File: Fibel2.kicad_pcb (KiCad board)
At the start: 2 copper layers, 210 x 148 mm, 0 parts

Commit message: added symbol&footprint for orin/sodimm, added a bunch of specs and docs, partially implemented audio, full steam ahead
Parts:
- added C1: 0.1uF, Capacitor_SMD:C_0603_1608Metric, F.Cu at (119.4, 76.9)
- added C10: 10uF, Capacitor_SMD:C_0603_1608Metric, F.Cu at (123.4, 84.5)
- added C11: 10uF, Capacitor_SMD:C_0603_1608Metric, F.Cu at (123.4, 87.0)
- added C12: 0.1uF, Capacitor_SMD:C_0603_1608Metric, F.Cu at (123.4, 89.5)
- added C13: 10uF, Capacitor_SMD:C_0603_1608Metric, F.Cu at (127.4, 76.9)
- added C14: 10uF, Capacitor_SMD:C_0603_1608Metric, F.Cu at (127.4, 79.4)
- added C15: 10uF, Capacitor_SMD:C_0603_1608Metric, F.Cu at (127.4, 81.9)
- added C16: 10uF, Capacitor_SMD:C_0603_1608Metric, F.Cu at (127.4, 84.5)
- added C17: 10uF, Capacitor_SMD:C_0603_1608Metric, F.Cu at (127.4, 87.0)
- added C18: 10uF, Capacitor_SMD:C_0603_1608Metric, F.Cu at (127.4, 89.5)
- added C19: 10uF, Capacitor_SMD:C_0603_1608Metric, F.Cu at (131.4, 76.9)
- added C2: 0.1uF, Capacitor_SMD:C_0603_1608Metric, F.Cu at (119.4, 79.4)
- added C20: 10uF, Capacitor_SMD:C_0603_1608Metric, F.Cu at (131.4, 79.4)
- added C21: 10uF, Capacitor_SMD:C_0603_1608Metric, F.Cu at (90.5, 76.9)
- added C22: 22uF, Capacitor_SMD:C_0805_2012Metric, F.Cu at (90.7, 99.8)
- added C23: 22uF, Capacitor_SMD:C_0805_2012Metric, F.Cu at (90.7, 102.8)
- added C24: 330uF, Capacitor_Tantalum_SMD:CP_EIA-6032-15_Kemet-U, F.Cu at (78.0, 142.0)
- added C25: 22uF, Capacitor_SMD:C_0805_2012Metric, F.Cu at (90.7, 105.8)
- added C26: 22uF, Capacitor_SMD:C_0805_2012Metric, F.Cu at (90.7, 108.8)
- added C27: 22uF, Capacitor_SMD:C_0805_2012Metric, F.Cu at (90.7, 111.8)
- added C28: 10uF, Capacitor_SMD:C_0603_1608Metric, F.Cu at (90.5, 79.4)
- added C29: 10uF, Capacitor_SMD:C_0603_1608Metric, F.Cu at (90.5, 81.9)
- added C3: 0.1uF, Capacitor_SMD:C_0603_1608Metric, F.Cu at (119.4, 81.9)
- added C30: 0.1uF, Capacitor_SMD:C_0603_1608Metric, F.Cu at (90.5, 84.5)
- added C31: 10uF, Capacitor_SMD:C_0603_1608Metric, F.Cu at (90.5, 87.0)
- added C32: 10uF, Capacitor_SMD:C_0603_1608Metric, F.Cu at (90.5, 89.5)
- added C33: 0.1uF, Capacitor_SMD:C_0603_1608Metric, F.Cu at (90.5, 92.0)
- added C4: 10uF, Capacitor_SMD:C_0603_1608Metric, F.Cu at (119.4, 84.5)
- added C41: 100nF, Capacitor_SMD:C_0603_1608Metric, F.Cu at (165.2, 69.5)
- added C42: 100nF, Capacitor_SMD:C_0603_1608Metric, F.Cu at (165.2, 72.0)
- added C46: 100nF, Capacitor_SMD:C_0603_1608Metric, F.Cu at (165.2, 74.5)
- added C47: 10uF, Capacitor_SMD:C_0603_1608Metric, F.Cu at (165.2, 77.0)
- added C48: 100nF, Capacitor_SMD:C_0603_1608Metric, F.Cu at (165.2, 79.5)
- added C5: 10uF, Capacitor_SMD:C_0603_1608Metric, F.Cu at (119.4, 87.0)
- added C50: 10uF, Capacitor_SMD:C_0603_1608Metric, F.Cu at (165.2, 82.0)
- added C6: 47nF, Capacitor_SMD:C_0603_1608Metric, F.Cu at (119.4, 89.5)
- added C61: 100nF, Capacitor_SMD:C_0603_1608Metric, F.Cu at (169.2, 69.5)
- added C62: 100nF, Capacitor_SMD:C_0603_1608Metric, F.Cu at (169.2, 72.0)
- added C63: 100nF, Capacitor_SMD:C_0603_1608Metric, F.Cu at (169.2, 74.5)
- added C7: 47nF, Capacitor_SMD:C_0603_1608Metric, F.Cu at (123.4, 76.9)
- added C8: 0.1uF, Capacitor_SMD:C_0603_1608Metric, F.Cu at (123.4, 79.4)
- added C9: 10uF, Capacitor_SMD:C_0603_1608Metric, F.Cu at (123.4, 81.9)
- added D1: BZT52Bxx, Diode_SMD:D_SOD-123F, F.Cu at (139.2, 92.4)
- added D2: BZT52Bxx, Diode_SMD:D_SOD-123F, F.Cu at (139.2, 95.8)
- added J1: Conn_02x20_Odd_Even, Connector_PinHeader_2.54mm:PinHeader_2x20_P2.54mm_Vertical, F.Cu at (98.0, 78.0)
- added J4: Conn_02x20_Odd_Even, Connector_PinHeader_2.54mm:PinHeader_2x20_P2.54mm_Vertical, F.Cu at (105.2, 78.0)
- added J5: Conn_01x02, Connector_JST:JST_EH_S2B-EH_1x02_P2.50mm_Horizontal, F.Cu at (120.9, 98.5)
- added J6: Conn_01x02, Connector_JST:JST_EH_S2B-EH_1x02_P2.50mm_Horizontal, F.Cu at (130.4, 98.5)
- added J7: Orin Nano, Fibel2:SODIMMx260, F.Cu at (72.5, 52.0)
- added Q1: CSD17581Q3A, Package_SON:VSON-8_3.3x3.3mm_P0.65mm_NexFET, F.Cu at (114.8, 78.2)
- added Q2: CSD17581Q3A, Package_SON:VSON-8_3.3x3.3mm_P0.65mm_NexFET, F.Cu at (114.8, 83.1)
- added Q3: CSD17581Q3A, Package_SON:VSON-8_3.3x3.3mm_P0.65mm_NexFET, F.Cu at (114.8, 88.1)
- added Q4: CSD17581Q3A, Package_SON:VSON-8_3.3x3.3mm_P0.65mm_NexFET, F.Cu at (114.8, 93.0)
- added R1: 294R, Resistor_SMD:R_0603_1608Metric, F.Cu at (131.4, 81.9)
- added R10: 127K, Resistor_SMD:R_0603_1608Metric, F.Cu at (135.4, 89.5)
- added R11: 100K, Resistor_SMD:R_0603_1608Metric, F.Cu at (90.5, 94.5)
- added R12: 100K, Resistor_SMD:R_0603_1608Metric, F.Cu at (90.5, 97.0)
- added R2: 294R, Resistor_SMD:R_0603_1608Metric, F.Cu at (131.4, 84.5)
- added R23: 10R, Resistor_SMD:R_0603_1608Metric, F.Cu at (169.2, 77.0)
- added R24: 10R, Resistor_SMD:R_0603_1608Metric, F.Cu at (169.2, 79.5)
- added R25: 10R, Resistor_SMD:R_0603_1608Metric, F.Cu at (169.2, 82.0)
- added R26: 10R, Resistor_SMD:R_0603_1608Metric, F.Cu at (173.2, 69.5)
- added R28: 10R, Resistor_SMD:R_0603_1608Metric, F.Cu at (173.2, 72.0)
- added R29: 4.7K, Resistor_SMD:R_0603_1608Metric, F.Cu at (173.2, 74.5)
- added R3: 10K, Resistor_SMD:R_0603_1608Metric, F.Cu at (131.4, 87.0)
- added R30: 4.7K, Resistor_SMD:R_0603_1608Metric, F.Cu at (173.2, 77.0)
- added R4: 6.04K, Resistor_SMD:R_0603_1608Metric, F.Cu at (131.4, 89.5)
- added R5: 127K, Resistor_SMD:R_0603_1608Metric, F.Cu at (135.4, 76.9)
- added R6: 100K, Resistor_SMD:R_0603_1608Metric, F.Cu at (135.4, 79.4)
- added R7: 100R, Resistor_SMD:R_0603_1608Metric, F.Cu at (135.4, 81.9)
- added R8: 5.24K, Resistor_SMD:R_0603_1608Metric, F.Cu at (135.4, 84.5)
- added R9: 30.31K, Resistor_SMD:R_0603_1608Metric, F.Cu at (135.4, 87.0)
- added U1: BQ25798RQMR, Fibel2:IBQ25798RQMR, F.Cu at (169.2, 121.4)
- added U2: TPS61022RWUR, Fibel2:TPS61022RWUR, F.Cu at (131.0, 143.2)
- added U3: rpi_pico, Fibel2:RPi Pico, F.Cu at (44.7, 115.1)
- added U4: WM8960CGEFL, Fibel2:QFN50P500X500X100-33N, F.Cu at (151.6, 131.2)
- added U5: TLV75718PDBV, Package_TO_SOT_SMD:SOT-23-5, F.Cu at (91.1, 115.7)
- added U6: TLV75733PDBV, Package_TO_SOT_SMD:SOT-23-5, F.Cu at (91.1, 120.3)

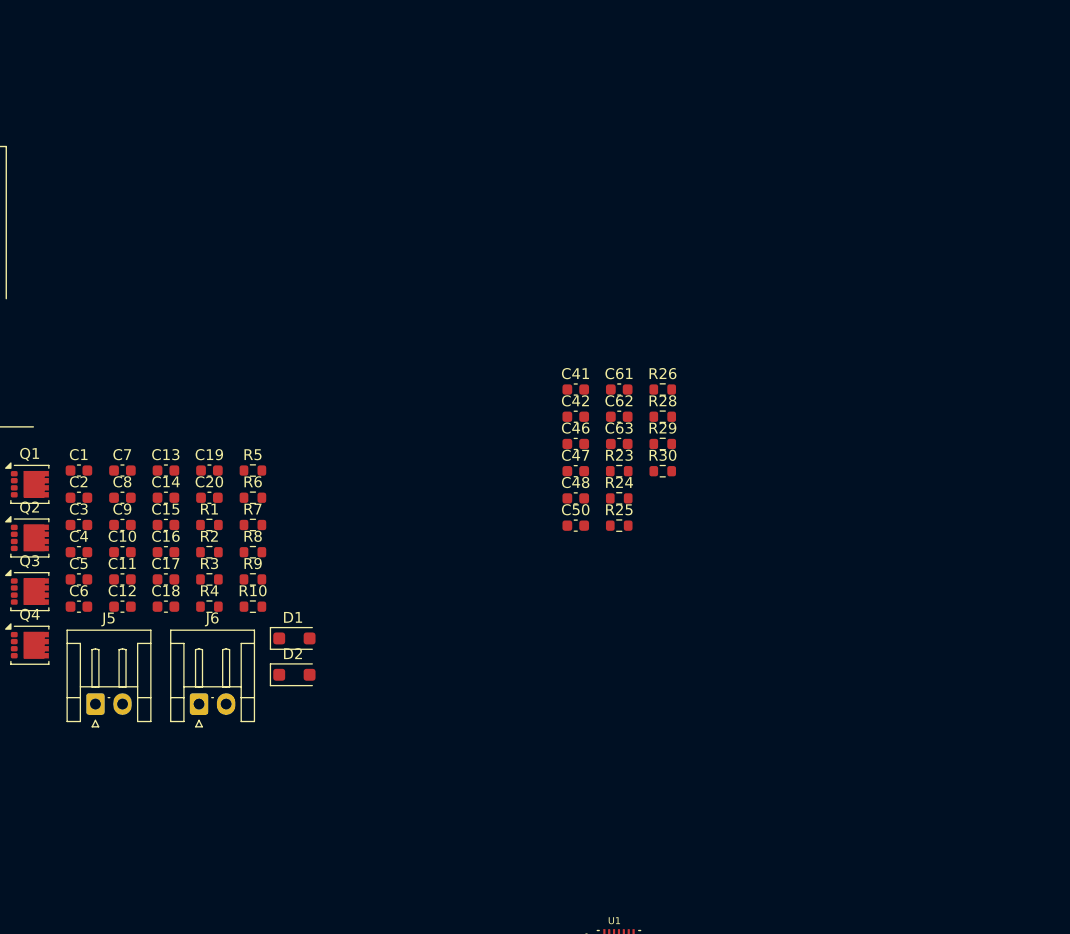
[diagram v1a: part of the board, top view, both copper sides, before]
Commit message: added usb+PD+DP & pcie implementations from antmicro design, added specs for USB components, rethought power+usb arch
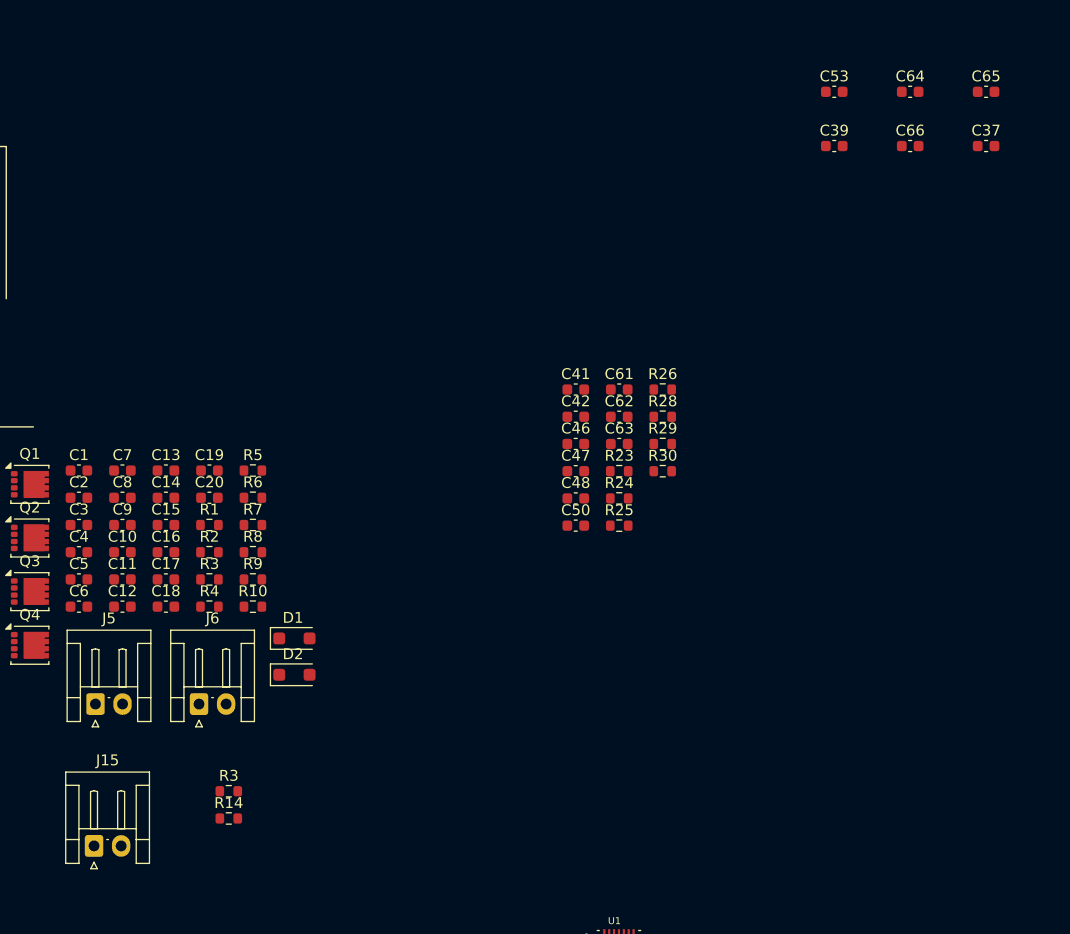
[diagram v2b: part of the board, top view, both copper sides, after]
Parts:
- added C37: 100pF, Capacitor_SMD:C_0603_1608Metric, F.Cu at (203.0, 47.0)
- added C39: 100pF, Capacitor_SMD:C_0603_1608Metric, F.Cu at (189.0, 47.0)
- added C53: 680nF DNP, Capacitor_SMD:C_0603_1608Metric, F.Cu at (189.0, 42.0)
- added C64: 100pF, Capacitor_SMD:C_0603_1608Metric, F.Cu at (196.0, 42.0)
- added C65: 100pF, Capacitor_SMD:C_0603_1608Metric, F.Cu at (203.0, 42.0)
- added C66: 680nF DNP, Capacitor_SMD:C_0603_1608Metric, F.Cu at (196.0, 47.0)
- added J15: Conn_01x02, Connector_JST:JST_EH_S2B-EH_1x02_P2.50mm_Horizontal, F.Cu at (120.8, 111.5)
- added R14: TBD/DNP, Resistor_SMD:R_0603_1608Metric, F.Cu at (133.2, 109.0)
- added R3: TBD/DNP, Resistor_SMD:R_0603_1608Metric, F.Cu at (133.2, 106.5)
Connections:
- net Net-(P2-D+) renamed /Charging/CHG_DN
- net Net-(P2-D-) renamed /Charging/CHG_DP
- net Net-(Q3-D) renamed VBUS_CHG
- net VCC renamed VSYS
- J6 pad 2: GND -> Net-(J15-Pin_1)
- U4 pad 19: unconnected-(U4-SPK_RN-Pad19) -> Net-(U4-SPK_RN)
- U4 pad 20: Net-(U4-AGND) -> GND
- U4 pad 22: unconnected-(U4-SPK_RP-Pad22) -> Net-(U4-SPK_RP)
- U4 pad 23: unconnected-(U4-SPK_LN-Pad23) -> Net-(U4-SPK_LN)
- U4 pad 24: Net-(U4-AGND) -> GND
- U4 pad 25: unconnected-(U4-SPK_LP-Pad25) -> Net-(U4-SPK_LP)
- U4 pad 28: Net-(U4-AGND) -> GND
- U4 pad 29: unconnected-(U4-HP_R-Pad29) -> /Audio/HPR
- U4 pad 31: unconnected-(U4-HP_L-Pad31) -> /Audio/HPL
- U4 pad 33: Net-(U4-AGND) -> GND
- U4 pad 9: Net-(U4-AGND) -> GND

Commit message: added footprint, symbol and model for TPS65987
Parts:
- added U8: TPS65988DHRSHR, Fibel2:IC_TPS65987DDHRSHR, F.Cu at (187.7, 103.4)

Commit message: added nets for 40 pin headers (epd & rpi header) connected some of the nets i'm reeusing
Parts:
- removed J1: Conn_02x20_Odd_Even, Connector_PinHeader_2.54mm:PinHeader_2x20_P2.54mm_Vertical
- removed J7: Orin Nano, Fibel2:SODIMMx260
- added C1001: 220nF, Capacitor_SMD:C_0603_1608Metric, F.Cu at (154.2, 37.4)
- added C1002: 220nF, Capacitor_SMD:C_0603_1608Metric, F.Cu at (154.2, 39.9)
- added C1003: 220nF, Capacitor_SMD:C_0603_1608Metric, F.Cu at (154.2, 42.4)
- added C1004: 220nF, Capacitor_SMD:C_0603_1608Metric, F.Cu at (154.2, 44.9)
- added C1005: 220nF, Capacitor_SMD:C_0603_1608Metric, F.Cu at (154.2, 47.5)
- added C1006: 220nF, Capacitor_SMD:C_0603_1608Metric, F.Cu at (154.2, 50.0)
- added C1007: 220nF, Capacitor_SMD:C_0603_1608Metric, F.Cu at (158.2, 37.4)
- added C1008: 220nF, Capacitor_SMD:C_0603_1608Metric, F.Cu at (158.2, 39.9)
- added C1009: 20uF, Capacitor_SMD:C_0603_1608Metric, F.Cu at (158.2, 42.4)
- added C1010: 20uF, Capacitor_SMD:C_0603_1608Metric, F.Cu at (158.2, 44.9)
- added C1011: 20uF, Capacitor_SMD:C_0603_1608Metric, F.Cu at (158.2, 47.5)
- added C1012: 20uF, Capacitor_SMD:C_0603_1608Metric, F.Cu at (158.2, 50.0)
- added C401: 10uF, Capacitor_SMD:C_0603_1608Metric, F.Cu at (120.1, 20.4)
- added C402: 100nF, Capacitor_SMD:C_0603_1608Metric, F.Cu at (120.1, 22.9)
- added C403: 10uF, Capacitor_SMD:C_0603_1608Metric, F.Cu at (120.1, 25.4)
- added C404: 10uF, Capacitor_SMD:C_0603_1608Metric, F.Cu at (120.1, 30.4)
- added C405: 10uF, Capacitor_SMD:C_0603_1608Metric, F.Cu at (120.1, 27.9)
- added C406: 10uF 25V, Capacitor_SMD:C_0603_1608Metric, F.Cu at (120.1, 32.9)
- added C407: 100nF, Capacitor_SMD:C_0603_1608Metric, F.Cu at (120.1, 35.4)
- added C408: 100nF, Capacitor_SMD:C_0603_1608Metric, F.Cu at (120.1, 37.9)
- added C409: 100nF, Capacitor_SMD:C_0603_1608Metric, F.Cu at (120.1, 40.4)
- added C410: 100nF, Capacitor_SMD:C_0603_1608Metric, F.Cu at (120.1, 48.0)
- added C411: 100nF, Capacitor_SMD:C_0603_1608Metric, F.Cu at (120.1, 53.0)
- added C412: 4.7uF, Capacitor_SMD:C_0603_1608Metric, F.Cu at (124.1, 22.9)
- added C413: 10uF, Capacitor_SMD:C_0603_1608Metric, F.Cu at (124.1, 25.4)
- added C414: 100nF, Capacitor_SMD:C_0603_1608Metric, F.Cu at (120.1, 45.5)
- added C415: 100nF, Capacitor_SMD:C_0603_1608Metric, F.Cu at (120.1, 50.5)
- added C416: 100nF, Capacitor_SMD:C_0603_1608Metric, F.Cu at (124.1, 20.4)
- added C417: 100nF, Capacitor_SMD:C_0603_1608Metric, F.Cu at (124.1, 27.9)
- added C418: 100nF, Capacitor_SMD:C_0603_1608Metric, F.Cu at (124.1, 30.4)
- added C419: 100nF, Capacitor_SMD:C_0603_1608Metric, F.Cu at (124.1, 32.9)
- added C420: 100nF, Capacitor_SMD:C_0603_1608Metric, F.Cu at (124.1, 35.4)
- added C421: 100nF, Capacitor_SMD:C_0603_1608Metric, F.Cu at (124.1, 37.9)
- added C422: 10uF, Capacitor_SMD:C_0603_1608Metric, F.Cu at (124.1, 40.4)
- added C423: 47pF, Capacitor_SMD:C_0603_1608Metric, F.Cu at (124.1, 42.9)
- added C424: 47pF, Capacitor_SMD:C_0603_1608Metric, F.Cu at (124.1, 45.5)
- added C425: 100nF, Capacitor_SMD:C_0603_1608Metric, F.Cu at (124.1, 48.0)
- added C426: 100nF, Capacitor_SMD:C_0603_1608Metric, F.Cu at (124.1, 50.5)
- added C427: 4.7uF, Capacitor_SMD:C_0603_1608Metric, F.Cu at (128.1, 22.9)
- added C428: 10uF, Capacitor_SMD:C_0603_1608Metric, F.Cu at (128.1, 30.4)
- added C429: 100nF, Capacitor_SMD:C_0603_1608Metric, F.Cu at (128.1, 32.9)
- added C430: 100nF, Capacitor_SMD:C_0603_1608Metric, F.Cu at (124.1, 53.0)
- added C431: 100nF, Capacitor_SMD:C_0603_1608Metric, F.Cu at (128.1, 20.4)
- added C432: 100nF, Capacitor_SMD:C_0603_1608Metric, F.Cu at (128.1, 25.4)
- added C433: 100nF, Capacitor_SMD:C_0603_1608Metric, F.Cu at (128.1, 27.9)
- added C434: 1uF 16V, Capacitor_SMD:C_0603_1608Metric, F.Cu at (128.1, 35.4)
- added C435: 100nF, Capacitor_SMD:C_0603_1608Metric, F.Cu at (120.1, 42.9)
- added C436: 100nF, Capacitor_SMD:C_0603_1608Metric, F.Cu at (128.1, 37.9)
- added C437: 1uF 16V, Capacitor_SMD:C_0603_1608Metric, F.Cu at (128.1, 40.4)
- added C701: 100uF 10V, Capacitor_SMD:C_0805_2012Metric, F.Cu at (166.4, 20.6)
- added C702: 100uF 10V, Capacitor_SMD:C_0805_2012Metric, F.Cu at (166.4, 23.6)
- added C703: 100pF, Capacitor_SMD:C_0603_1608Metric, F.Cu at (158.2, 32.9)
- added C704: 100pF, Capacitor_SMD:C_0603_1608Metric, F.Cu at (162.2, 20.4)
- added C716: 100nF, Capacitor_SMD:C_0603_1608Metric, F.Cu at (154.2, 32.9)
- added C721: 10uF, Capacitor_SMD:C_0603_1608Metric, F.Cu at (154.2, 20.4)
- added C722: 10uF, Capacitor_SMD:C_0603_1608Metric, F.Cu at (158.2, 20.4)
- added C723: 100nF, Capacitor_SMD:C_0603_1608Metric, F.Cu at (154.2, 22.9)
- added C724: 100nF, Capacitor_SMD:C_0603_1608Metric, F.Cu at (158.2, 22.9)
- added C725: 33pF, Capacitor_SMD:C_0603_1608Metric, F.Cu at (154.2, 25.4)
- added C726: 33pF, Capacitor_SMD:C_0603_1608Metric, F.Cu at (158.2, 25.4)
- added C727: 33pF, Capacitor_SMD:C_0603_1608Metric, F.Cu at (154.2, 27.9)
- added C728: 33pF, Capacitor_SMD:C_0603_1608Metric, F.Cu at (158.2, 27.9)
- added C729: 10uF, Capacitor_SMD:C_0603_1608Metric, F.Cu at (154.2, 30.4)
- added C730: 10uF, Capacitor_SMD:C_0603_1608Metric, F.Cu at (158.2, 30.4)
- added C901: 220nF, Capacitor_SMD:C_0603_1608Metric, F.Cu at (154.2, 54.5)
- added C902: 220nF, Capacitor_SMD:C_0603_1608Metric, F.Cu at (154.2, 57.0)
- added C903: 20uF, Capacitor_SMD:C_0603_1608Metric, F.Cu at (154.2, 59.5)
- added C904: 20uF, Capacitor_SMD:C_0603_1608Metric, F.Cu at (154.2, 62.0)
- added D303: LED, Capacitor_SMD:C_0603_1608Metric, F.Cu at (120.1, 57.5)
- added J1201: Orin Nano, Fibel2:SODIMMx260, F.Cu at (24.1, 96.9)
- added J2: Bus_M.2_Socket_M, Capacitor_SMD:C_0603_1608Metric, F.Cu at (162.2, 37.4)
- added J501: Conn_02x20_Odd_Even, Connector_PinHeader_2.54mm:PinHeader_2x20_P2.54mm_Vertical, F.Cu at (80.5, 29.1)
- added J702: SPK_JST_L, Capacitor_SMD:C_0603_1608Metric, F.Cu at (162.2, 25.4)
- added J703: SPK_JST_R, Capacitor_SMD:C_0603_1608Metric, F.Cu at (162.2, 22.9)
- added L301: 1uH, Resistor_SMD:R_0603_1608Metric, F.Cu at (120.1, 60.0)
- added R1001: 47K, Resistor_SMD:R_0603_1608Metric, F.Cu at (162.2, 39.9)
- added R1002: 47K, Resistor_SMD:R_0603_1608Metric, F.Cu at (162.2, 42.4)
- added R1003: 200R, Resistor_SMD:R_0603_1608Metric, F.Cu at (162.2, 44.9)
- added R1004: 0R 22A, Resistor_SMD:R_0603_1608Metric, F.Cu at (162.2, 47.5)
- added R401: 10K, Resistor_SMD:R_0603_1608Metric, F.Cu at (175.2, 20.0)
- added R402: 100K, Resistor_SMD:R_0603_1608Metric, F.Cu at (175.2, 22.5)
- added R403: 10K, Resistor_SMD:R_0603_1608Metric, F.Cu at (175.2, 25.0)
- added R404: 100K, Resistor_SMD:R_0603_1608Metric, F.Cu at (175.2, 27.5)
- added R405: 0R, Resistor_SMD:R_0603_1608Metric, F.Cu at (175.2, 30.0)
- added R406: 10K, Resistor_SMD:R_0603_1608Metric, F.Cu at (175.2, 32.5)
- added R407: 0R, Resistor_SMD:R_0603_1608Metric, F.Cu at (128.1, 48.0)
- added R408: 0R, Resistor_SMD:R_0603_1608Metric, F.Cu at (128.1, 50.5)
- added R409: 0R, Resistor_SMD:R_0603_1608Metric, F.Cu at (128.1, 53.0)
- added R410: 0R, Resistor_SMD:R_0603_1608Metric, F.Cu at (132.1, 20.4)
- added R411: 0R, Resistor_SMD:R_0603_1608Metric, F.Cu at (136.1, 22.9)
- added R412: 10K, Resistor_SMD:R_0603_1608Metric, F.Cu at (136.1, 27.9)
- added R413: 0R, Resistor_SMD:R_0603_1608Metric, F.Cu at (136.1, 30.4)
- added R415: 10K, Resistor_SMD:R_0603_1608Metric, F.Cu at (136.1, 32.9)
- added R416: 0R, Resistor_SMD:R_0603_1608Metric, F.Cu at (132.1, 27.9)
- added R417: 200R, Resistor_SMD:R_0603_1608Metric, F.Cu at (132.1, 30.4)
- added R418: 200R, Resistor_SMD:R_0603_1608Metric, F.Cu at (132.1, 32.9)
- added R419: 0R, Resistor_SMD:R_0603_1608Metric, F.Cu at (132.1, 35.4)
- added R420: 0R, Resistor_SMD:R_0603_1608Metric, F.Cu at (132.1, 37.9)
- added R421: 0R, Resistor_SMD:R_0603_1608Metric, F.Cu at (132.1, 40.4)
- added R422: 200R, Resistor_SMD:R_0603_1608Metric, F.Cu at (132.1, 42.9)
- added R423: 200R, Resistor_SMD:R_0603_1608Metric, F.Cu at (132.1, 45.5)
- added R424: 2.2K, Resistor_SMD:R_0603_1608Metric, F.Cu at (136.1, 40.4)
- added R425: 27R, Resistor_SMD:R_0603_1608Metric, F.Cu at (136.1, 42.9)
- added R426: 27R, Resistor_SMD:R_0603_1608Metric, F.Cu at (136.1, 45.5)
- added R427: 0R, Resistor_SMD:R_0603_1608Metric, F.Cu at (148.1, 25.4)
- added R428: 0R, Resistor_SMD:R_0603_1608Metric, F.Cu at (148.1, 27.9)
- added R429: 100K, Resistor_SMD:R_0603_1608Metric, F.Cu at (132.1, 53.0)
- added R430: 100K, Resistor_SMD:R_0603_1608Metric, F.Cu at (136.1, 20.4)
- added R431: 0R, Resistor_SMD:R_0603_1608Metric, F.Cu at (144.1, 53.0)
- added R432: 0R, Resistor_SMD:R_0603_1608Metric, F.Cu at (136.1, 25.4)
- added R433: 0R, Resistor_SMD:R_0603_1608Metric, F.Cu at (148.1, 20.4)
- added R434: 0R, Resistor_SMD:R_0603_1608Metric, F.Cu at (148.1, 22.9)
- added R435: 4.7K, Resistor_SMD:R_0603_1608Metric, F.Cu at (132.1, 48.0)
- added R436: 4.7K, Resistor_SMD:R_0603_1608Metric, F.Cu at (132.1, 50.5)
- added R437: 4.7K, Resistor_SMD:R_0603_1608Metric, F.Cu at (132.1, 22.9)
- added R438: 4.7K, Resistor_SMD:R_0603_1608Metric, F.Cu at (132.1, 25.4)
- added R439: 0R, Resistor_SMD:R_0603_1608Metric, F.Cu at (148.1, 30.4)
- added R440: 0R, Resistor_SMD:R_0603_1608Metric, F.Cu at (136.1, 35.4)
- added R441: 0R, Resistor_SMD:R_0603_1608Metric, F.Cu at (136.1, 37.9)
- added R442: 0R, Resistor_SMD:R_0603_1608Metric, F.Cu at (148.1, 32.9)
- added R443: 10K, Resistor_SMD:R_0603_1608Metric, F.Cu at (136.1, 48.0)
- added R444: 0R, Resistor_SMD:R_0603_1608Metric, F.Cu at (140.1, 50.5)
- added R445: 0R, Resistor_SMD:R_0603_1608Metric, F.Cu at (140.1, 53.0)
- added R446: 10K, Resistor_SMD:R_0603_1608Metric, F.Cu at (144.1, 20.4)
- added R447: 2K, Resistor_SMD:R_0603_1608Metric, F.Cu at (136.1, 50.5)
- added R448: 1K, Resistor_SMD:R_0603_1608Metric, F.Cu at (136.1, 53.0)
- added R449: 2K, Resistor_SMD:R_0603_1608Metric, F.Cu at (140.1, 20.4)
- added R450: 2K, Resistor_SMD:R_0603_1608Metric, F.Cu at (140.1, 22.9)
- added R451: 2K, Resistor_SMD:R_0603_1608Metric, F.Cu at (140.1, 25.4)
- added R452: 1K, Resistor_SMD:R_0603_1608Metric, F.Cu at (140.1, 27.9)
- added R453: 2K, Resistor_SMD:R_0603_1608Metric, F.Cu at (140.1, 30.4)
- added R454: 2K, Resistor_SMD:R_0603_1608Metric, F.Cu at (140.1, 32.9)
- added R455: 2K, Resistor_SMD:R_0603_1608Metric, F.Cu at (140.1, 35.4)
- added R456: 1K, Resistor_SMD:R_0603_1608Metric, F.Cu at (140.1, 37.9)
- added R457: 2K, Resistor_SMD:R_0603_1608Metric, F.Cu at (140.1, 40.4)
- added R458: 2K, Resistor_SMD:R_0603_1608Metric, F.Cu at (140.1, 42.9)
- added R459: 2K, Resistor_SMD:R_0603_1608Metric, F.Cu at (140.1, 45.5)
- added R460: 1K, Resistor_SMD:R_0603_1608Metric, F.Cu at (140.1, 48.0)
- added R461: 2.2K, Resistor_SMD:R_0603_1608Metric, F.Cu at (144.1, 25.4)
- added R462: 4.7K, Resistor_SMD:R_0603_1608Metric, F.Cu at (144.1, 22.9)
- added R463: 0R, Resistor_SMD:R_0603_1608Metric, F.Cu at (144.1, 40.4)
- added R464: 0R, Resistor_SMD:R_0603_1608Metric, F.Cu at (144.1, 42.9)
- added R465: 1K, Resistor_SMD:R_0603_1608Metric, F.Cu at (175.2, 35.0)
- added R466: 0R, Resistor_SMD:R_0603_1608Metric, F.Cu at (144.1, 45.5)
- added R467: 0R, Resistor_SMD:R_0603_1608Metric, F.Cu at (144.1, 35.4)
- added R468: 0R, Resistor_SMD:R_0603_1608Metric, F.Cu at (144.1, 37.9)
- added R469: 0R, Resistor_SMD:R_0603_1608Metric, F.Cu at (128.1, 45.5)
- added R470: 0R, Resistor_SMD:R_0603_1608Metric, F.Cu at (128.1, 42.9)
- added R471: 0R, Resistor_SMD:R_0603_1608Metric, F.Cu at (144.1, 48.0)
- added R472: 0R, Resistor_SMD:R_0603_1608Metric, F.Cu at (144.1, 50.5)
- added R473: 3M, Resistor_SMD:R_0603_1608Metric, F.Cu at (144.1, 27.9)
- added R474: 3M, Resistor_SMD:R_0603_1608Metric, F.Cu at (144.1, 30.4)
- added R475: 4.7K, Resistor_SMD:R_0603_1608Metric, F.Cu at (144.1, 32.9)
- added R708: 10k, Resistor_SMD:R_0603_1608Metric, F.Cu at (181.2, 22.5)
- added R709: 10k, Resistor_SMD:R_0603_1608Metric, F.Cu at (181.2, 25.0)
- added R710: 10k, Resistor_SMD:R_0603_1608Metric, F.Cu at (181.2, 20.0)
- added R903: 47K, Resistor_SMD:R_0603_1608Metric, F.Cu at (158.2, 57.0)
- added R904: 0R, Resistor_SMD:R_0603_1608Metric, F.Cu at (154.2, 64.5)
- added R905: 0R, Resistor_SMD:R_0603_1608Metric, F.Cu at (158.2, 54.5)
- added R906: 47K, Resistor_SMD:R_0603_1608Metric, F.Cu at (158.2, 59.5)
- added R907: 200R, Resistor_SMD:R_0603_1608Metric, F.Cu at (158.2, 62.0)
- added R908: 0R, Resistor_SMD:R_0603_1608Metric, F.Cu at (158.2, 64.5)
- added R909: 0R, Resistor_SMD:R_0603_1608Metric, F.Cu at (162.2, 54.5)
- added R910: 0R, Resistor_SMD:R_0603_1608Metric, F.Cu at (162.2, 57.0)
- added R911: 47K, Resistor_SMD:R_0603_1608Metric, F.Cu at (162.2, 59.5)
- added R912: 200R, Resistor_SMD:R_0603_1608Metric, F.Cu at (162.2, 62.0)
- added TH301: 10K, Resistor_SMD:R_0603_1608Metric, F.Cu at (120.1, 62.5)
- added TP1001: TP_0.75mm_SMD, TestPoint:TestPoint_Pad_D1.0mm, F.Cu at (211.0, 62.9)
- added TP1002: TP_0.75mm_SMD, TestPoint:TestPoint_Pad_D1.0mm, F.Cu at (211.0, 66.0)
- added TP1003: TP_0.75mm_SMD, TestPoint:TestPoint_Pad_D1.0mm, F.Cu at (211.0, 69.0)
- added TP401: TP_0.75mm_SMD, TestPoint:TestPoint_Pad_D1.0mm, F.Cu at (194.8, 62.9)
- added TP402: TP_0.75mm_SMD, TestPoint:TestPoint_Pad_D1.0mm, F.Cu at (194.8, 66.0)
- added TP403: TP_0.75mm_SMD, TestPoint:TestPoint_Pad_D1.0mm, F.Cu at (200.9, 66.0)
- added TP404: TP_0.75mm_SMD, TestPoint:TestPoint_Pad_D1.0mm, F.Cu at (194.8, 69.0)
- added TP405: TP_0.75mm_SMD, TestPoint:TestPoint_Pad_D1.0mm, F.Cu at (194.8, 72.0)
- added TP406: TP_0.75mm_SMD, TestPoint:TestPoint_Pad_D1.0mm, F.Cu at (197.8, 62.9)
- added TP407: TP_0.75mm_SMD, TestPoint:TestPoint_Pad_D1.0mm, F.Cu at (197.8, 66.0)
- added TP408: TP_0.75mm_SMD, TestPoint:TestPoint_Pad_D1.0mm, F.Cu at (197.8, 69.0)
- added TP409: TP_0.75mm_SMD, TestPoint:TestPoint_Pad_D1.0mm, F.Cu at (197.8, 72.0)
- added TP410: TP_0.75mm_SMD, TestPoint:TestPoint_Pad_D1.0mm, F.Cu at (200.9, 62.9)
- added TP411: TP_0.75mm_SMD, TestPoint:TestPoint_Pad_D1.0mm, F.Cu at (200.9, 69.0)
- added TP901: TP_0.75mm_SMD, TestPoint:TestPoint_Pad_D1.0mm, F.Cu at (205.9, 62.9)
- added TP902: TP_0.75mm_SMD, TestPoint:TestPoint_Pad_D1.0mm, F.Cu at (205.9, 66.0)
- added TP903: TP_0.75mm_SMD, TestPoint:TestPoint_Pad_D1.0mm, F.Cu at (205.9, 69.0)
- added TP904: TP_0.75mm_SMD, TestPoint:TestPoint_Pad_D1.0mm, F.Cu at (205.9, 72.0)
- moved U601 217.9 mm to (252.3, 49.1)
- moved J801 49.7 mm to (98.0, 28.8)
- renumbered C21 to C201, C26 to C202, C27 to C203, C28 to C204, C31 to C205, C29 to C206, C32 to C207, C22 to C208, C30 to C209, C33 to C210, C23 to C211, C25 to C212, C24 to C213, C1 to C301, C2 to C302, C3 to C303, C4 to C304, C6 to C305, C7 to C306, C5 to C307, C20 to C308, C12 to C309, C8 to C310, C18 to C311, C13 to C312, C9 to C313, C19 to C314, C14 to C315, C10 to C316, C15 to C317, C11 to C318, C16 to C319, C17 to C320, C64 to C705, C37 to C706, C61 to C707, C65 to C708, C39 to C709, C62 to C710, C66 to C711, C53 to C712, C63 to C713, C48 to C714, C50 to C715, C41 to C717, C42 to C718, C46 to C719, C47 to C720, D1 to D301, D2 to D302, J5 to J301, J6 to J302, J15 to J303, J4 to J801, Q1 to Q301, Q3 to Q302, Q2 to Q303, Q4 to Q304, R11 to R201, R12 to R202, R1 to R301, R2 to R302, R4 to R303, R8 to R304, R9 to R305, R7 to R306, R5 to R307, R6 to R308, R10 to R309, R30 to R701, R29 to R702, R23 to R703, R24 to R704, R25 to R705, R26 to R706, R28 to R707, U5 to U201, U6 to U202, U2 to U203, U1 to U301, U8 to U402, U3 to U601, U4 to U701
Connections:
- J801 pad 1: unconnected-(J4-Pin_1-Pad1) -> D3V3
- J801 pad 10: unconnected-(J4-Pin_10-Pad10) -> UART1_RXD
- J801 pad 12: unconnected-(J4-Pin_12-Pad12) -> I2S0_SCLK
- J801 pad 14: unconnected-(J4-Pin_14-Pad14) -> GND
- J801 pad 15: unconnected-(J4-Pin_15-Pad15) -> GPIO12
- J801 pad 17: unconnected-(J4-Pin_17-Pad17) -> D3V3
- J801 pad 19: unconnected-(J4-Pin_19-Pad19) -> SPI0_MOSI
- J801 pad 2: unconnected-(J4-Pin_2-Pad2) -> VDD_MOD
- J801 pad 20: unconnected-(J4-Pin_20-Pad20) -> GND
- J801 pad 21: unconnected-(J4-Pin_21-Pad21) -> SPI0_MISO
- J801 pad 23: unconnected-(J4-Pin_23-Pad23) -> SPI0_SCK
- J801 pad 24: unconnected-(J4-Pin_24-Pad24) -> SPI0_CS0
- J801 pad 25: unconnected-(J4-Pin_25-Pad25) -> GND
- J801 pad 26: unconnected-(J4-Pin_26-Pad26) -> SPI0_CS1
- J801 pad 29: unconnected-(J4-Pin_29-Pad29) -> GPIO01
- J801 pad 3: unconnected-(J4-Pin_3-Pad3) -> I2C1_SDA
- J801 pad 30: unconnected-(J4-Pin_30-Pad30) -> GND
- J801 pad 31: unconnected-(J4-Pin_31-Pad31) -> GPIO11
- J801 pad 32: unconnected-(J4-Pin_32-Pad32) -> GPIO07
- J801 pad 33: unconnected-(J4-Pin_33-Pad33) -> GPIO13
- J801 pad 34: unconnected-(J4-Pin_34-Pad34) -> GND
- J801 pad 35: unconnected-(J4-Pin_35-Pad35) -> I2S0_FS
- J801 pad 38: unconnected-(J4-Pin_38-Pad38) -> I2S0_DIN
- J801 pad 39: unconnected-(J4-Pin_39-Pad39) -> GND
- J801 pad 4: unconnected-(J4-Pin_4-Pad4) -> VDD_MOD
- J801 pad 40: unconnected-(J4-Pin_40-Pad40) -> I2S0_DOUT
- J801 pad 5: unconnected-(J4-Pin_5-Pad5) -> I2C1_SCL
- J801 pad 6: unconnected-(J4-Pin_6-Pad6) -> GND
- J801 pad 7: unconnected-(J4-Pin_7-Pad7) -> GPIO09
- J801 pad 8: unconnected-(J4-Pin_8-Pad8) -> UART1_TXD
- J801 pad 9: unconnected-(J4-Pin_9-Pad9) -> GND
- U301 pad 6: /Charging/CHG_DP -> CHG_DP
- U301 pad 7: /Charging/CHG_DN -> CHG_DN

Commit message: restructured EPD side of things, replaced rp2040 with esp32 s3 because of it's LCD controller, USB, LP WIFI_BT & EPDiy compat, repurposed USB0 for ESP interfacing, added e-ink pmic
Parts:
- removed U601: rpi_pico, Fibel2:RPi Pico
- added U1: IT8951, Fibel2:QFP40P1600X1600X160-128N, F.Cu at (192.5, 128.5)
- added U2: TPS651851RSLT, Fibel2:IC_TPS651851, F.Cu at (197.2, 148.7)
- added U3: MX25L3206EM2I-12G, Fibel2:SOIC127P790X216-8N, F.Cu at (166.6, 148.6)
- added U4: ESP32-S3-WROOM-1U, Fibel2:XCVR_ESP32-S3-WROOM-1U, F.Cu at (37.8, 34.9)
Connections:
- J1201 pad 101: unconnected-(J1201B-UART0_RXD-Pad101) -> UART0_RXD
- J1201 pad 103: unconnected-(J1201B-UART0_RTS-Pad103) -> UART0_TXD
- J1201 pad 105: unconnected-(J1201B-UART0_CTS-Pad105) -> UART0_CTS
- J1201 pad 131: unconnected-(J1201B-PCIE0_RX0_N-Pad131) -> PCIE0_RX0_N
- J1201 pad 133: unconnected-(J1201B-PCIE0_RX0_P-Pad133) -> PCIE0_RX0_P
- J1201 pad 134: unconnected-(J1201B-PCIE0_TX0_N-Pad134) -> PCIE0_TX0_N
- J1201 pad 136: unconnected-(J1201B-PCIE0_TX0_P-Pad136) -> PCIE0_TX0_P
- J1201 pad 137: unconnected-(J1201B-PCIE0_RX1_N-Pad137) -> PCIE0_RX1_N
- J1201 pad 139: unconnected-(J1201B-PCIE0_RX1_P-Pad139) -> PCIE0_RX1_P
- J1201 pad 140: unconnected-(J1201B-PCIE0_TX1_N-Pad140) -> PCIE0_TX1_N
- J1201 pad 142: unconnected-(J1201B-PCIE0_TX1_P-Pad142) -> PCIE0_TX1_P
- J1201 pad 148: unconnected-(J1201C-PCIE0_TX2_N-Pad148) -> PCIE0_TX2_N
- J1201 pad 149: unconnected-(J1201C-PCIE0_RX2_N-Pad149) -> PCIE0_RX2_N
- J1201 pad 150: unconnected-(J1201C-PCIE0_TX2_P-Pad150) -> PCIE0_TX2_P
- J1201 pad 151: unconnected-(J1201C-PCIE0_RX2_P-Pad151) -> PCIE0_RX2_P
- J1201 pad 154: unconnected-(J1201C-PCIE0_TX3_N-Pad154) -> PCIE0_TX3_N
- J1201 pad 155: unconnected-(J1201C-PCIE0_RX3_N-Pad155) -> PCIE0_RX3_N
- J1201 pad 156: unconnected-(J1201C-PCIE0_TX3_P-Pad156) -> PCIE0_TX3_P
- J1201 pad 157: unconnected-(J1201C-PCIE0_RX3_P-Pad157) -> PCIE0_RX3_P
- J1201 pad 160: unconnected-(J1201C-PCIE0_CLK_N-Pad160) -> PCIE0_CLK_N
- J1201 pad 162: unconnected-(J1201C-PCIE0_CLK_P-Pad162) -> PCIE0_CLK_P
- J1201 pad 167: unconnected-(J1201C-PCIE1_RX0_N-Pad167) -> PCIE1_RX0_N
- J1201 pad 169: unconnected-(J1201C-PCIE1_RX0_P-Pad169) -> PCIE1_RX0_P
- J1201 pad 172: unconnected-(J1201C-PCIE1_TX0_N-Pad172) -> PCIE1_TX0_N
- J1201 pad 173: unconnected-(J1201C-PCIE1_CLK_N-Pad173) -> PCIE1_CLK_N
- J1201 pad 174: unconnected-(J1201C-PCIE1_TX0_P-Pad174) -> PCIE1_TX0_P
- J1201 pad 175: unconnected-(J1201C-PCIE1_CLK_P-Pad175) -> PCIE1_CLK_P
- J1201 pad 180: unconnected-(J1201C-PCIE0_CLKREQ-Pad180) -> PCIE0_CLKREQ*
- J1201 pad 181: unconnected-(J1201C-PCIE0_RST-Pad181) -> PCIE0_RST*
- J1201 pad 182: unconnected-(J1201C-PCIE1_CLKREQ-Pad182) -> PCIE1_CLKREQ*
- J1201 pad 183: unconnected-(J1201C-PCIE1_RST-Pad183) -> PCIE1_RST*
- J1201 pad 185: unconnected-(J1201C-I2C0_SCL-Pad185) -> SYS_SCL
- J1201 pad 187: unconnected-(J1201C-I2C0_SDA-Pad187) -> SYS_SDA
- J1201 pad 189: unconnected-(J1201C-I2C1_SCL-Pad189) -> PWR_SCL
- J1201 pad 191: unconnected-(J1201C-I2C1_SDA-Pad191) -> PWR_SDA
- J1201 pad 193: unconnected-(J1201C-I2S0_DOUT-Pad193) -> I2S0_DOUT
- J1201 pad 195: unconnected-(J1201C-I2S0_DIN-Pad195) -> I2S0_DIN
- J1201 pad 197: unconnected-(J1201C-I2S0_FS-Pad197) -> I2S0_FS
- J1201 pad 199: unconnected-(J1201C-I2S0_SCLK-Pad199) -> I2S0_SCLK
- J1201 pad 220: unconnected-(J1201D-I2S1_DOUT-Pad220) -> I2S1_DOUT
- J1201 pad 222: unconnected-(J1201D-I2S1_DIN-Pad222) -> I2S1_SDIN
- J1201 pad 224: unconnected-(J1201D-I2S1_FS-Pad224) -> I2S1_LRCK
- J1201 pad 226: unconnected-(J1201D-I2S1_SCLK-Pad226) -> I2S1_SCLK
- J1201 pad 236: unconnected-(J1201D-UART2_TXD-Pad236) -> DEBUG_RXD
- J1201 pad 238: unconnected-(J1201D-UART2_RXD-Pad238) -> DEBUG_TXD
- J1201 pad 99: unconnected-(J1201B-UART0_TXD-Pad99) -> UART0_RTS
- R420 pad 1: SYS_SCL -> PWR_SCL
- R421 pad 1: SYS_SDA -> PWR_SDA
- U301 pad 14: CHG_SCL -> PWR_SCL
- U301 pad 15: CHG_SDA -> PWR_SDA
